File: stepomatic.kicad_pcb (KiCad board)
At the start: 2 copper layers, 50 x 30 mm, 30 parts, among them J1 I2C, J2 Conn_01x05, J4 USB_B_Micro, Q1 MMBT3904, Q2 MMBT3904, SW1 Mode, SW2 RST, U1 HDC1080DMBR, U2 AMS1117-3.3, U3 ULN2003A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

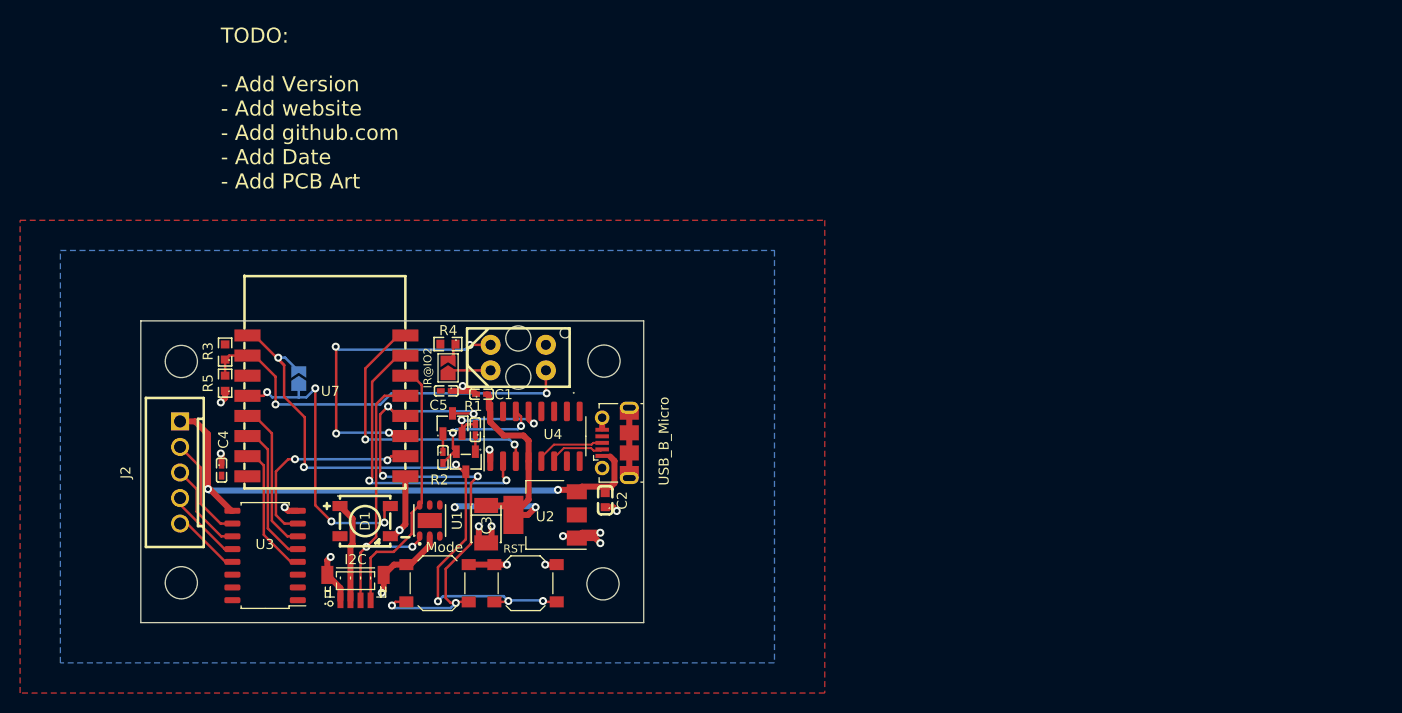
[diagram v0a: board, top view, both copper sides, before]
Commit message: Secure 3V3 connections and change the way the ADC is read
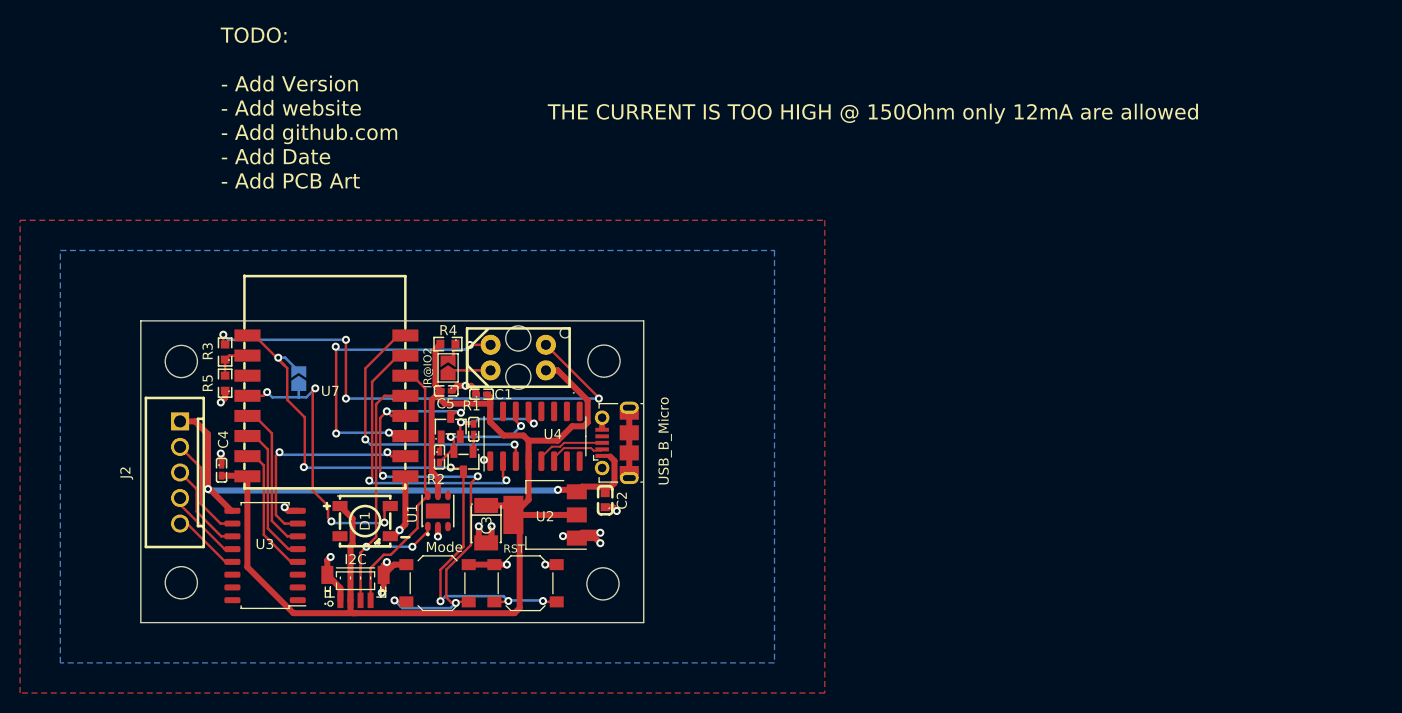
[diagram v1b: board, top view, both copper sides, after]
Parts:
- moved U1 1.25 mm to (129.5, 88.9)
- moved Q2 0.36 mm to (130.8, 80.5)
- moved R2 0.35 mm to (129.7, 83.5)
- moved Q1 0.23 mm to (132.1, 84.0)
- moved R1 0.17 mm to (133.1, 80.8)
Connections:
- CGQ1 pad 1: ADC -> +3V3
- CGQ1 pad 2: GND -> Net-(CGQ1-Pad2)
- R3 pad 2: +3V3 -> Net-(CGQ1-Pad2)
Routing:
- net +3V3: track 38.9 -> 122.8 mm, vias 2 -> 0
- net Net-(CGQ1-Pad2): track 0.00 -> 52.0 mm, vias 0 -> 4
- net ADC: track 40.1 -> 3.98 mm, vias 2 -> 0
- net GPIO0: track 54.1 -> 50.4 mm
- net GND: track 53.4 -> 51.4 mm, vias 16 -> 18
- net STEPPER4: track 20.4 -> 21.8 mm
- net I2C_SDA: track 29.3 -> 30.6 mm
- net RESET: track 63.8 -> 62.9 mm
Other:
- board text added: "THE CURRENT IS TOO HIGH @ 150Ohm only 12mA are allowed"

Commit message: Add 200k because of saturation voltage of the photo transistor
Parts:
- added C7: 10uF, footprint:C0402, F.Cu at (108.0, 81.8)
- R3: value 220k -> 200k
- R4: value 150 -> 220
- moved C4 0.47 mm to (107.9, 84.4), turned to 90 degrees
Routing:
- net Net-(CGQ1-Pad2): track 52.0 -> 46.4 mm
- net +3V3: track 122.8 -> 117.4 mm
- net +5V: track 55.9 -> 55.0 mm
- net GND: track 51.4 -> 52.1 mm, vias 18 -> 19

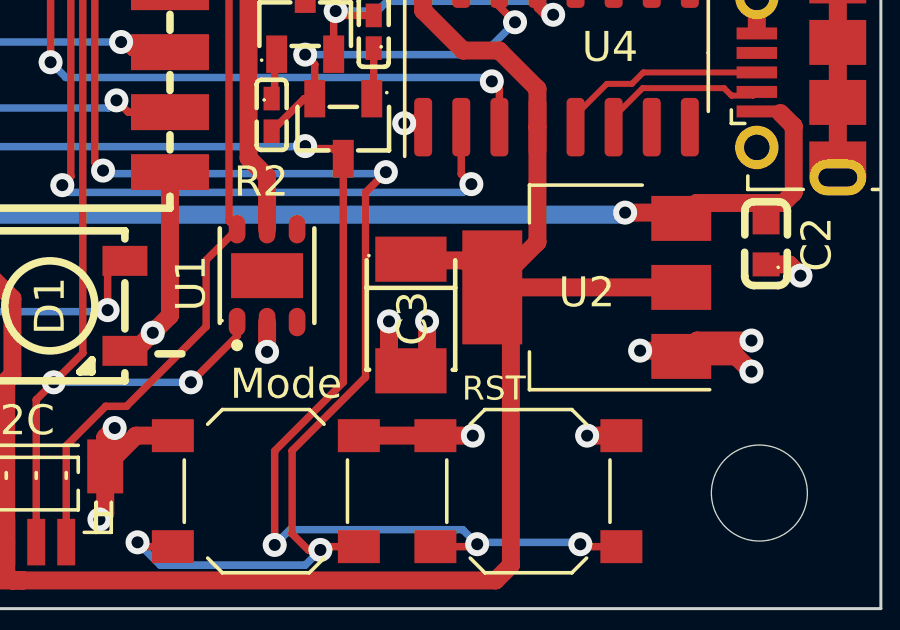
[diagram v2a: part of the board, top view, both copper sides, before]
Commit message: Include neopixel and fix package of C3 100uF
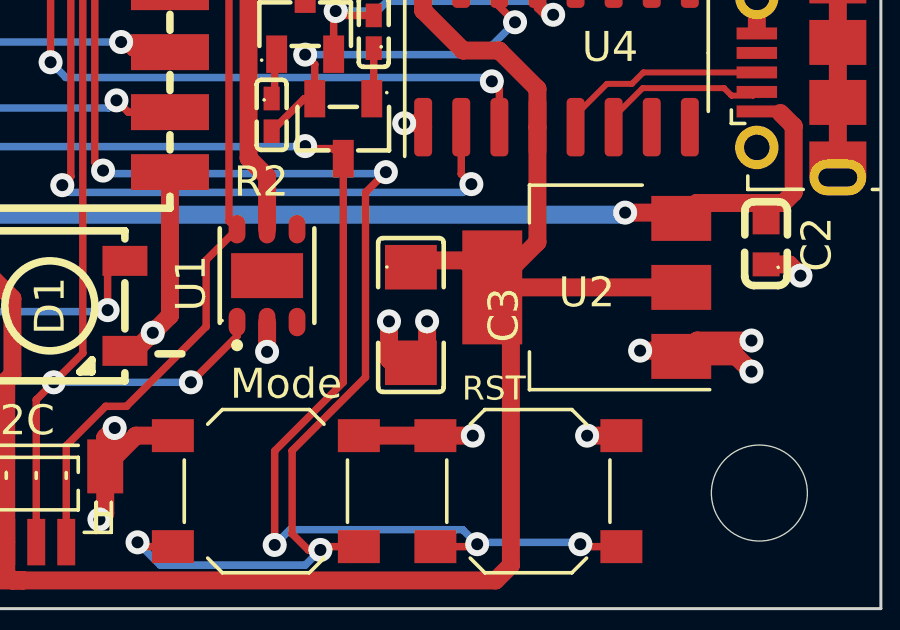
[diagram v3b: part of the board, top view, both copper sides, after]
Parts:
- C3: footprint footprint:CASE-B_3528 -> footprint:C1206
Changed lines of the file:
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@@
     (property "Sheetfile" "stepomatic.kicad_sch")
     (property "Sheetname" "")
-    (property "exclude_from_bom" "")
-    (attr smd exclude_from_bom)
+    (attr smd)
     (fp_text reference "D1" (at 0 0.000635 90) (layer "F.SilkS")
       (effects (font (size 1 1) (thickness 0.15)))
@@
     )
   )
-  (footprint "footprint:CASE-B_3528" (layer "F.Cu")
+  (footprint "footprint:C1206" (layer "F.Cu")
     (at 134.334912 90.212388 -90)
-    (descr "CASE-B_3528 footprint")
-    (tags "CASE-B_3528 footprint C16133")
+    (descr "C1206 footprint")
+    (tags "C1206 footprint C15008")
     (property "LCSC" "C15008")
     (property "Sheetfile" "stepomatic.kicad_sch")
     (property "Sheetname" "")
     (attr smd)
-    (fp_text reference "C3" (at 0.113851 -0.053441 90) (layer "F.SilkS")
-      (effects (font (size 1 1) (thickness 0.15)))
-    )
-    (fp_text value "100u" (at 0 3.4762 90) (layer "F.Fab")
-      (effects (font (size 1 1) (thickness 0.15)))
-    )
-    (fp_text user "REF**" (at 0 5.4762 90) (layer "F.Fab")
-      (effects (font (size 1 1) (thickness 0.15)))
-    )
-    (fp_line (start 1.826187 1.4762) (end 1.826187 1.391237) (layer "F.SilkS") (width 0.1524))
-    (fp_line (start 1.826187 -1.4762) (end -1.826187 -1.4762) (layer "F.SilkS") (width 0.1524))
-    (fp_line (start -0.904318 1.4762) (end -0.904318 -1.4762) (layer "F.SilkS") (width 0.1524))
-    (fp_line (start 1.826187 1.4762) (end -1.826187 1.4762) (layer "F.SilkS") (width 0.1524))
-    (fp_line (start 1.826187 -1.4762) (end 1.826187 -1.391237) (layer "F.SilkS") (width 0.1524))
-    (fp_circle (center -1.979934 1.400051) (end -1.949962 1.400051) (layer "F.SilkS") (width 0.059995) (fill none))
-    (pad "1" smd rect locked (at -1.860554 0 90) (size 1.506248 2.375997) (layers "F.Cu" "F.Paste" "F.Mask")
+    (fp_text reference "C3" (at 0 -3.092609 -90) (layer "F.SilkS")
+      (effects (font (size 1 1) (thickness 0.15)))
+    )
+    (fp_text value "100u" (at 0 3.092609 -90) (layer "F.Fab")
+      (effects (font (size 1 1) (thickness 0.15)))
+    )
+    (fp_text user "REF**" (at 0 5.092609 -90) (layer "F.Fab")
+      (effects (font (size 1 1) (thickness 0.15)))
+    )
+    (fp_line (start -0.926213 1.092609) (end -2.411201 1.092609) (layer "F.SilkS") (width 0.1524))
+    (fp_line (start -2.411201 -1.092609) (end -0.926213 -1.092609) (layer "F.SilkS") (width 0.1524))
+    (fp_line (start -2.563602 0.940208) (end -2.563602 -0.940208) (layer "F.SilkS") (width 0.1524))
+    (fp_line (start 0.926213 1.092609) (end 2.411201 1.092609) (layer "F.SilkS") (width 0.1524))
+    (fp_line (start 2.563602 0.940208) (end 2.563602 -0.940208) (layer "F.SilkS") (width 0.1524))
+    (fp_line (start 2.411201 -1.092609) (end 0.926213 -1.092609) (layer "F.SilkS") (width 0.1524))
+    (fp_arc (start -2.411201 1.092609) (mid -2.518965 1.047972) (end -2.563602 0.940208) (layer "F.SilkS") (width 0.1524))
+    (fp_arc (start 2.411201 -1.092609) (mid 2.518965 -1.047972) (end 2.563602 -0.940208) (layer "F.SilkS") (width 0.1524))
+    (fp_arc (start 2.563602 0.940208) (mid 2.518965 1.047972) (end 2.411201 1.092609) (layer "F.SilkS") (width 0.1524))
+    (fp_arc (start -2.563602 -0.940208) (mid -2.518965 -1.047972) (end -2.411201 -1.092609) (layer "F.SilkS") (width 0.1524))
+    (fp_circle (center -1.599949 0.800102) (end -1.569977 0.800102) (layer "F.SilkS") (width 0.059995) (fill none))
+    (pad "1" smd rect locked (at -1.592583 0 270) (size 1.485014 1.727991) (layers "F.Cu" "F.Paste" "F.Mask")
       (net 3 "+3V3") (pintype "passive"))
-    (pad "2" smd rect locked (at 1.860554 0 90) (size 1.506248 2.375997) (layers "F.Cu" "F.Paste" "F.Mask")
+    (pad "2" smd rect locked (at 1.592583 0 270) (size 1.485014 1.727991) (layers "F.Cu" "F.Paste" "F.Mask")
       (net 2 "GND") (pintype "passive"))
-    (model "lib/footprint/packages3d/CASE-B_3528.step"
-      (offset (xyz 0 0 0))
-      (scale (xyz 1 1 1))
+    (model "lib/footprint/packages3d/C1206.step"
+      (offset (xyz 0 0 0))
+      (scale (xyz 1 1 1))
